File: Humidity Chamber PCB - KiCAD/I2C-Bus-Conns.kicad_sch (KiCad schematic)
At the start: 14 parts, among them J10 MFC 3, J11 I2C_STANDARDQWIIC, J12 I2C_STANDARDQWIIC, J13 MFC 2, J14 MFC 4, J15 MFM 1, J16 MFM 2, J9 MFC 1

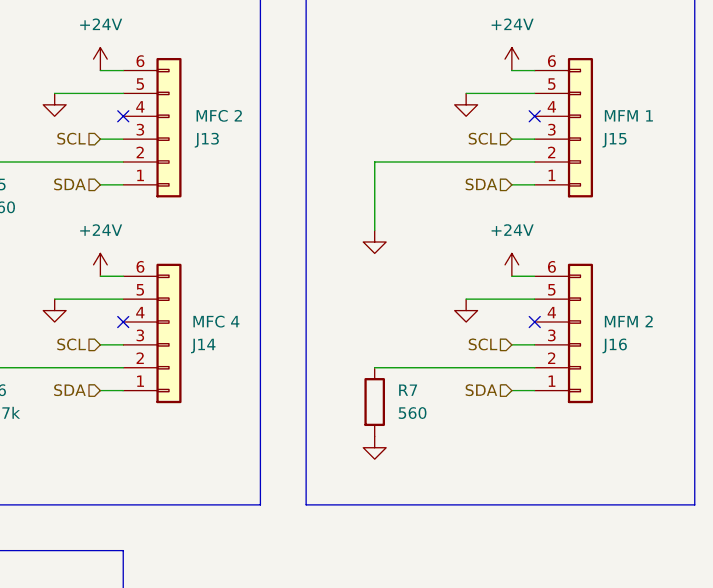
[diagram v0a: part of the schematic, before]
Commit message: Start v1.1.   Fix address resistors for MFMs
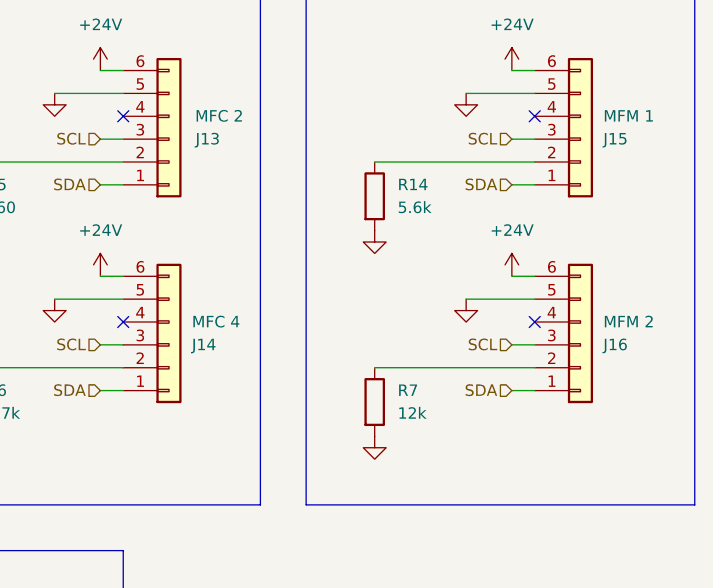
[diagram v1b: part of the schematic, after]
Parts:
- added R14: 5.6k, Resistor_THT:R_Axial_DIN0207_L6.3mm_D2.5mm_P10.16mm_Horizontal, symbol Device:R
- R7: value 560 -> 12k
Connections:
- net GND: now also R14.2; no longer J15.2 (Pin_2)
- new net: J15.2 (Pin_2), R14.1
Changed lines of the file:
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@@
 	(title_block
 		(title "Datta Lab Humidity Chamber Controller")
-		(date "2026-01-07")
-		(rev "1.0")
+		(date "2026-01-26")
+		(rev "1.1")
 		(company "HMS Research Instrumentation Core")
 	)
@@
 		(pts
 			(xy 124.46 40.64) (xy 132.08 40.64)
-		)
-		(stroke
-			(width 0)
-			(type default)
-		)
-	)
-	(wire
-		(pts
-			(xy 114.3 48.26) (xy 114.3 55.88)
 		)
 		(stroke
@@
 	)
 	(symbol
+		(lib_id "Device:R")
+		(at 114.3 52.07 0)
+		(unit 1)
+		(exclude_from_sim no)
+		(in_bom yes)
+		(on_board yes)
+		(dnp no)
+		(fields_autoplaced yes)
+		(property "Reference" "R14"
+			(at 116.84 50.7999 0)
+			(effects
+				(font
+					(size 1.27 1.27)
+				)
+				(justify left)
+			)
+		)
+		(property "Value" "5.6k"
+			(at 116.84 53.3399 0)
+			(effects
+				(font
+					(size 1.27 1.27)
+				)
+				(justify left)
+			)
+		)
+		(property "Footprint" "Resistor_THT:R_Axial_DIN0207_L6.3mm_D2.5mm_P10.16mm_Horizontal"
+			(at 112.522 52.07 90)
+			(effects
+				(font
+					(size 1.27 1.27)
+				)
+				(hide yes)
+			)
+		)
+		(property "Datasheet" "~"
+			(at 114.3 52.07 0)
+			(effects
+				(font
+					(size 1.27 1.27)
+				)
+				(hide yes)
+			)
+		)
+		(property "Description" "Resistor"
+			(at 114.3 52.07 0)
+			(effects
+				(font
+					(size 1.27 1.27)
+				)
+				(hide yes)
+			)
+		)
+		(pin "1"
+		)
+		(pin "2"
+		)
+		(instances
+			(project "Datta Lab Humidity Chamber PCB"
+				(path "/d7d8f86e-c8d6-438e-95be-a4e29dfe527f/29aff04f-5256-4a71-9320-1940ab24e10e"
+					(reference "R14")
+					(unit 1)
+				)
+				(path "/d7d8f86e-c8d6-438e-95be-a4e29dfe527f/424aee9d-cce1-4aae-b0be-0f762712ebda"
+					(reference "R15")
+					(unit 1)
+				)
+			)
+		)
+	)
+	(symbol
 		(lib_id "Connector_Generic:Conn_01x06")
 		(at 137.16 45.72 0)
@@
 			)
 		)
-		(property "Value" "560"
+		(property "Value" "12k"
 			(at 116.84 76.1999 0)
 			(effects
